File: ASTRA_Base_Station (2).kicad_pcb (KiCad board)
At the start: 2 copper layers, 34.9 x 38.8 mm, 21 parts, among them J2 24V, J3 24V, J4 24V, J5 5V, U4 D24V22F3, U5 D24V22F5

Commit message: Ground Plane Attempt
Attempted to add a ground plane, it only spawns for some components of the board. Looking into solution.
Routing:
- added copper zone on B.Cu, net GND
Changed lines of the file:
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@@
 		(embedded_fonts no)
+	)
+	(gr_rect
+		(start 143 20.5)
+		(end 249.5 153.5)
+		(stroke
+			(width 0.2)
+			(type default)
+		)
+		(fill no)
+		(layer "F.Cu")
 	)
 	(segment
@@
 		(net 10)
 		(net_name "GND")
-		(layer "F.Cu")
+		(layers "F.Cu" "B.Cu")
+		(name "GND")
 		(hatch edge 0.5)
 		(connect_pads
@@
 		(min_thickness 0.25)
 		(filled_areas_thickness no)
-		(fill
+		(fill yes
 			(thermal_gap 0.5)
 			(thermal_bridge_width 0.5)
@@
 		(polygon
 			(pts
-				(xy 145.907416 18.5) (xy 253 19.99) (xy 254.5 158.5) (xy 142.5 159.5) (xy 143 19.5) (xy 146 18.5)
+				(xy 143 20.5) (xy 249.5 20.5) (xy 249.5 153.5) (xy 143 153.5)
 			)
 		)

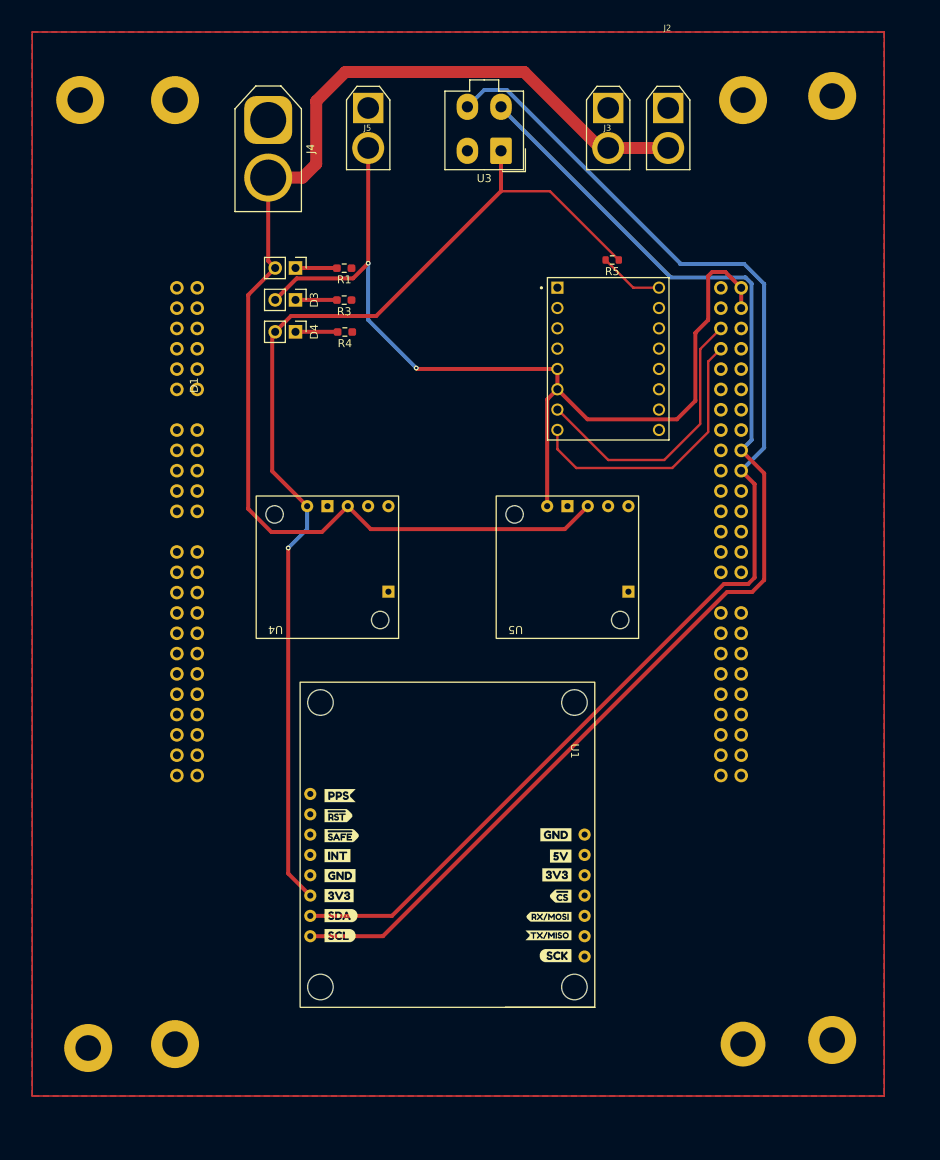
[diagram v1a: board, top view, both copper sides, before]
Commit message: PCB Review Draft
All  PCB connections made
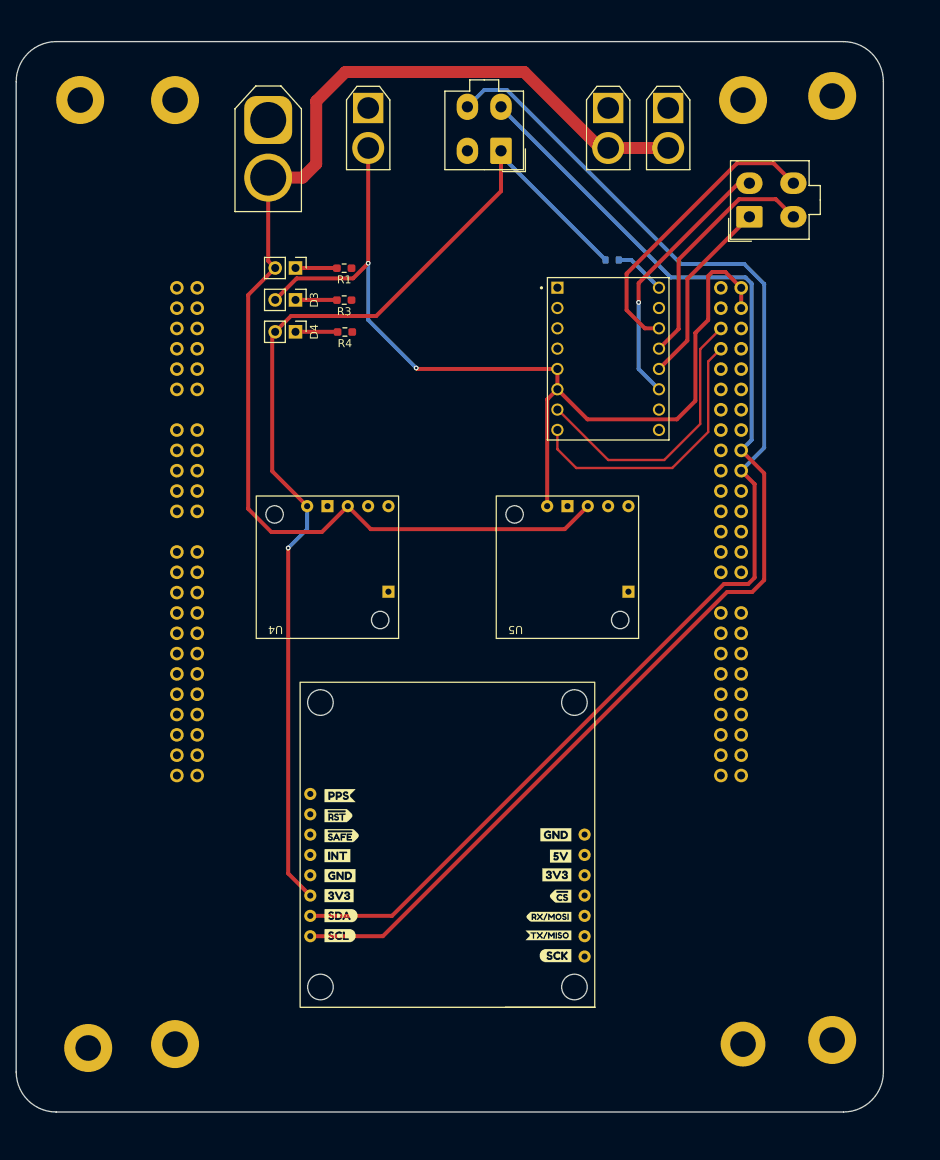
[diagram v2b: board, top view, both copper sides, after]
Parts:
- added M1: Stepper_Motor_bipolar, Connector_Molex:Molex_Mini-Fit_Jr_5566-04A_2x02_P4.20mm_Vertical, F.Cu at (232.7, 43.6)
- R5: value 176 mΩ -> 142 mΩ; moved to B.Cu
- turned R5 to 0 degrees
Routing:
- net /B2_Motor: track 0.00 -> 37.2 mm
- net /A2_Motor: track 0.00 -> 33.3 mm, vias 0 -> 1
- net /B1_Motor: track 0.00 -> 30.5 mm
- net /A1_Motor: track 0.00 -> 23.7 mm
- net Net-(1-VMOT): track 8.11 -> 6.46 mm
- net +3.3V: track 133.7 -> 134.2 mm
- removed copper zone on B.Cu, net GND
- removed copper zone on F.Cu, net GND
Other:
- board size 34.9 x 38.8 mm -> 108.4 x 133.8 mm
